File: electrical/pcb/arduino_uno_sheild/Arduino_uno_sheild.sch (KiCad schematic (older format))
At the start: 16 parts, among them J1 ED10523-ND, J2 6posheader, J3 6posheader, J4 6posheader, J5 6posheader, J6 ED2580-ND, y1 rover_silkscreen

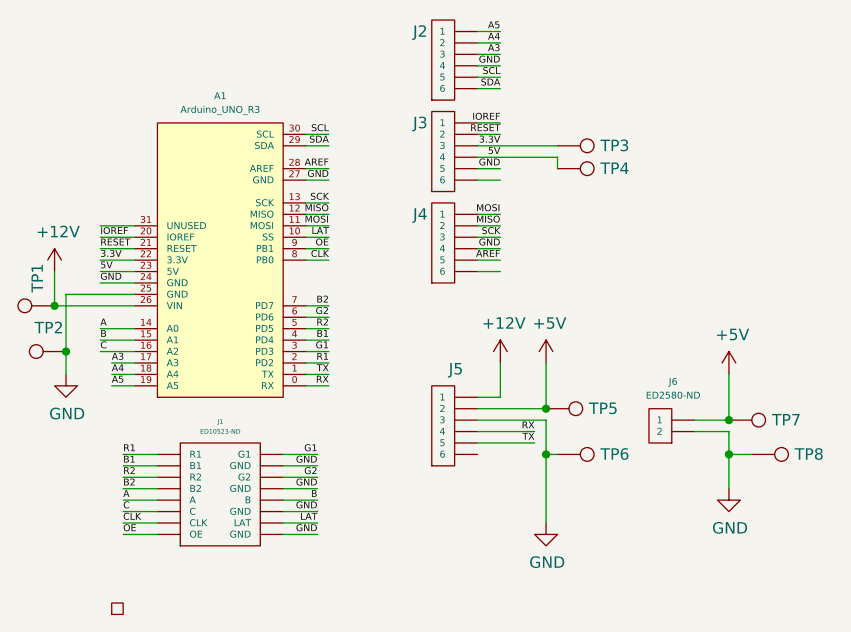
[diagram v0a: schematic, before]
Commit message: Updating raspberrypi-arduino communication to use i2c instead of usb/serial
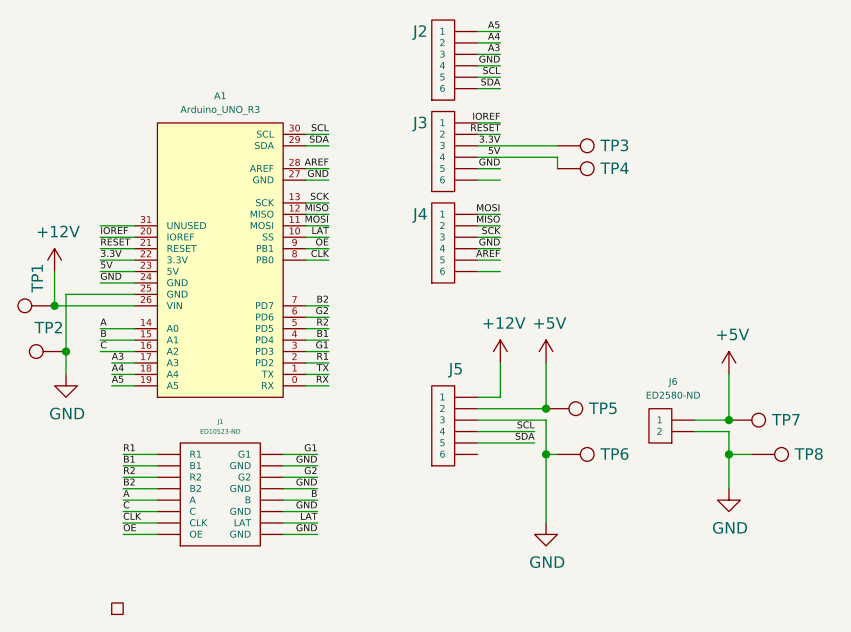
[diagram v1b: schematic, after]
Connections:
- net RX: no longer J5.4
- net SCL: now also J5.4
- net SDA: now also J5.5
- net TX: no longer J5.5
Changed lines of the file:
@@
 EESchema Schematic File Version 4
-LIBS:Arduino_uno_sheild-cache
-EELAYER 26 0
+EELAYER 30 0
 EELAYER END
 $Descr A4 11693 8268
@@
 	4100 3300 4350 3300
 Text Label 4350 3250 2    30   ~ 0
-RX
+SCL
 Text Label 4350 3300 2    30   ~ 0
-TX
+SDA
 Wire Wire Line
 	2250 2700 2600 2700
